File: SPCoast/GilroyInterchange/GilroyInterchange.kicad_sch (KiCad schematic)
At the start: 47 parts, among them SW783 783, SW795 795, SW799 799

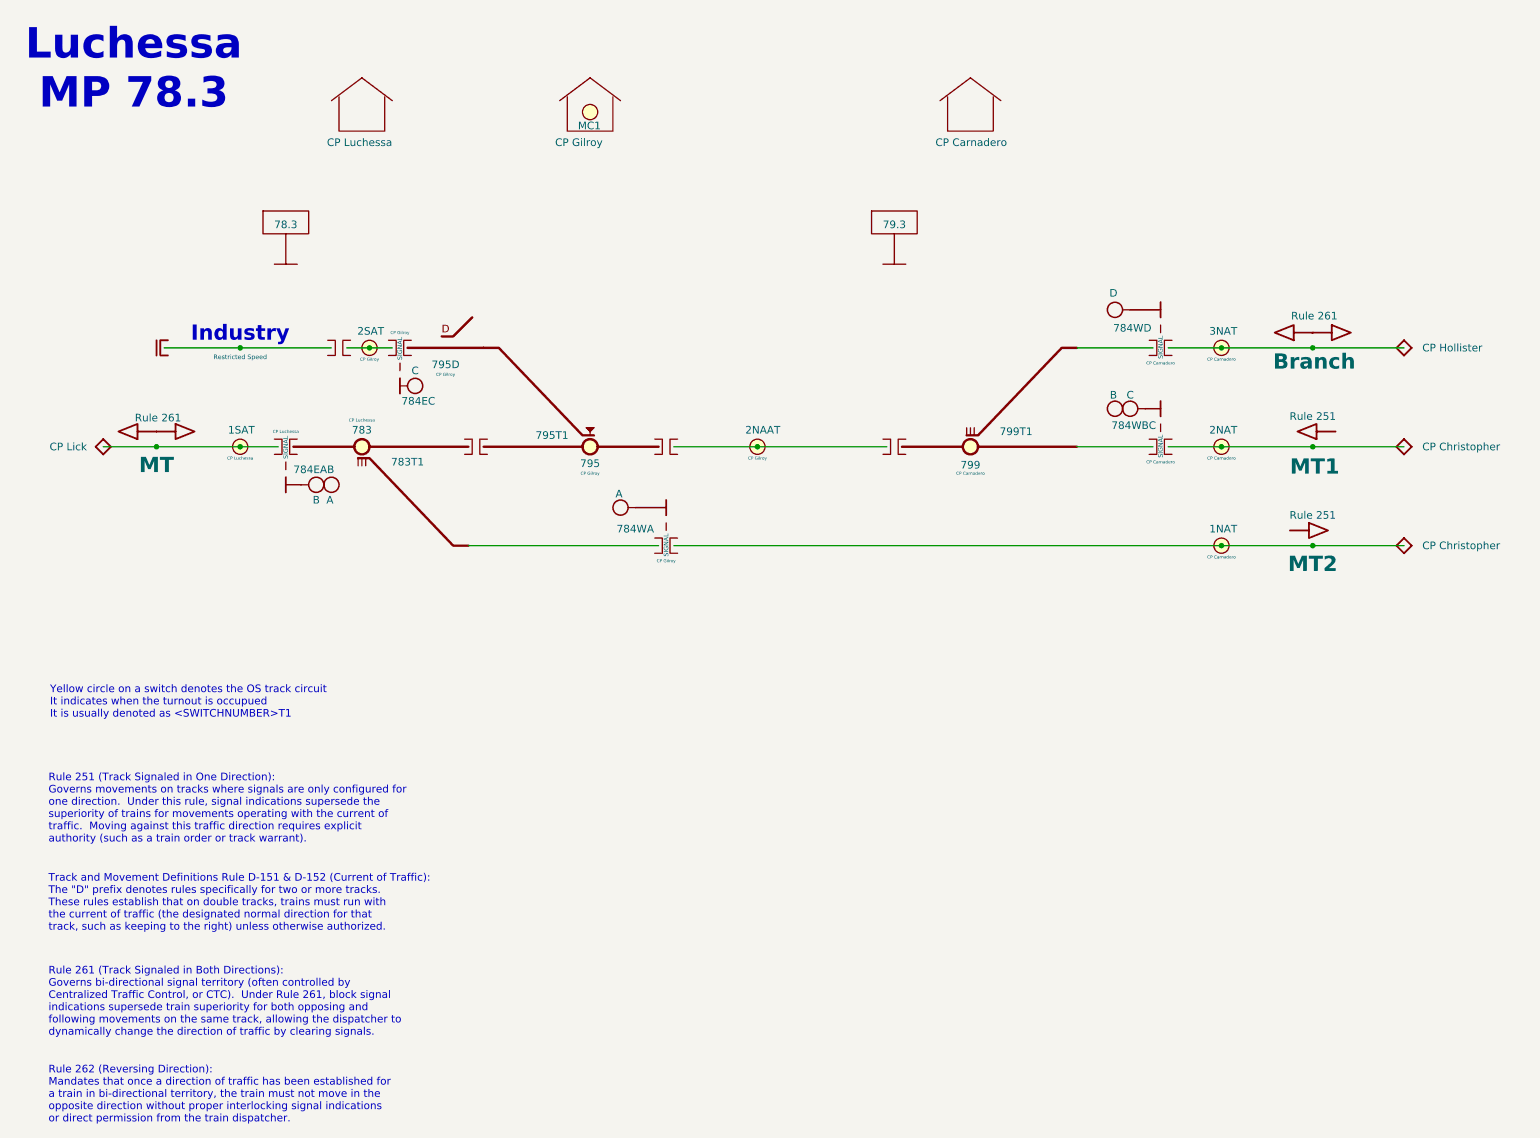
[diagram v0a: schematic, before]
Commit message: SPCoast: derail pin R, track circuit names end in T, code line symbols on the root sheet
Working-tree changes from the 2026-10-01..03 vocabulary review with
FieldUnit-Subdivision (docs/adr/0001-code-line-type-contract.md):

- Switch_Powered_Derail pin 2 is R (through path = REVERSE) in the seven
  plant schematics (library Railroad.kicad_sym renamed alongside; not in git)
- Luchessa track circuits renamed to end in T (1SAT, 2NAAT, ...); MC1 moved
  to CP Gilroy's house
- South-cTc: transports (MQTT, TimeCode, CMRInet, Loconet) on the root
  sheet on the CtcMachine Transports pin; field stations as encoding
  instances on the Luchessa sheet; two Luchessa lamp tokens renamed
- Six plant projects (Christopher, Corporal, GilroyCalTrain,
  GilroyInterchange, Sargent, Watsonville) added as drawn so far; Watsonville
  updated 2026-10-02

Co-Authored-By: Claude Fable 5.1 <noreply@anthropic.com>
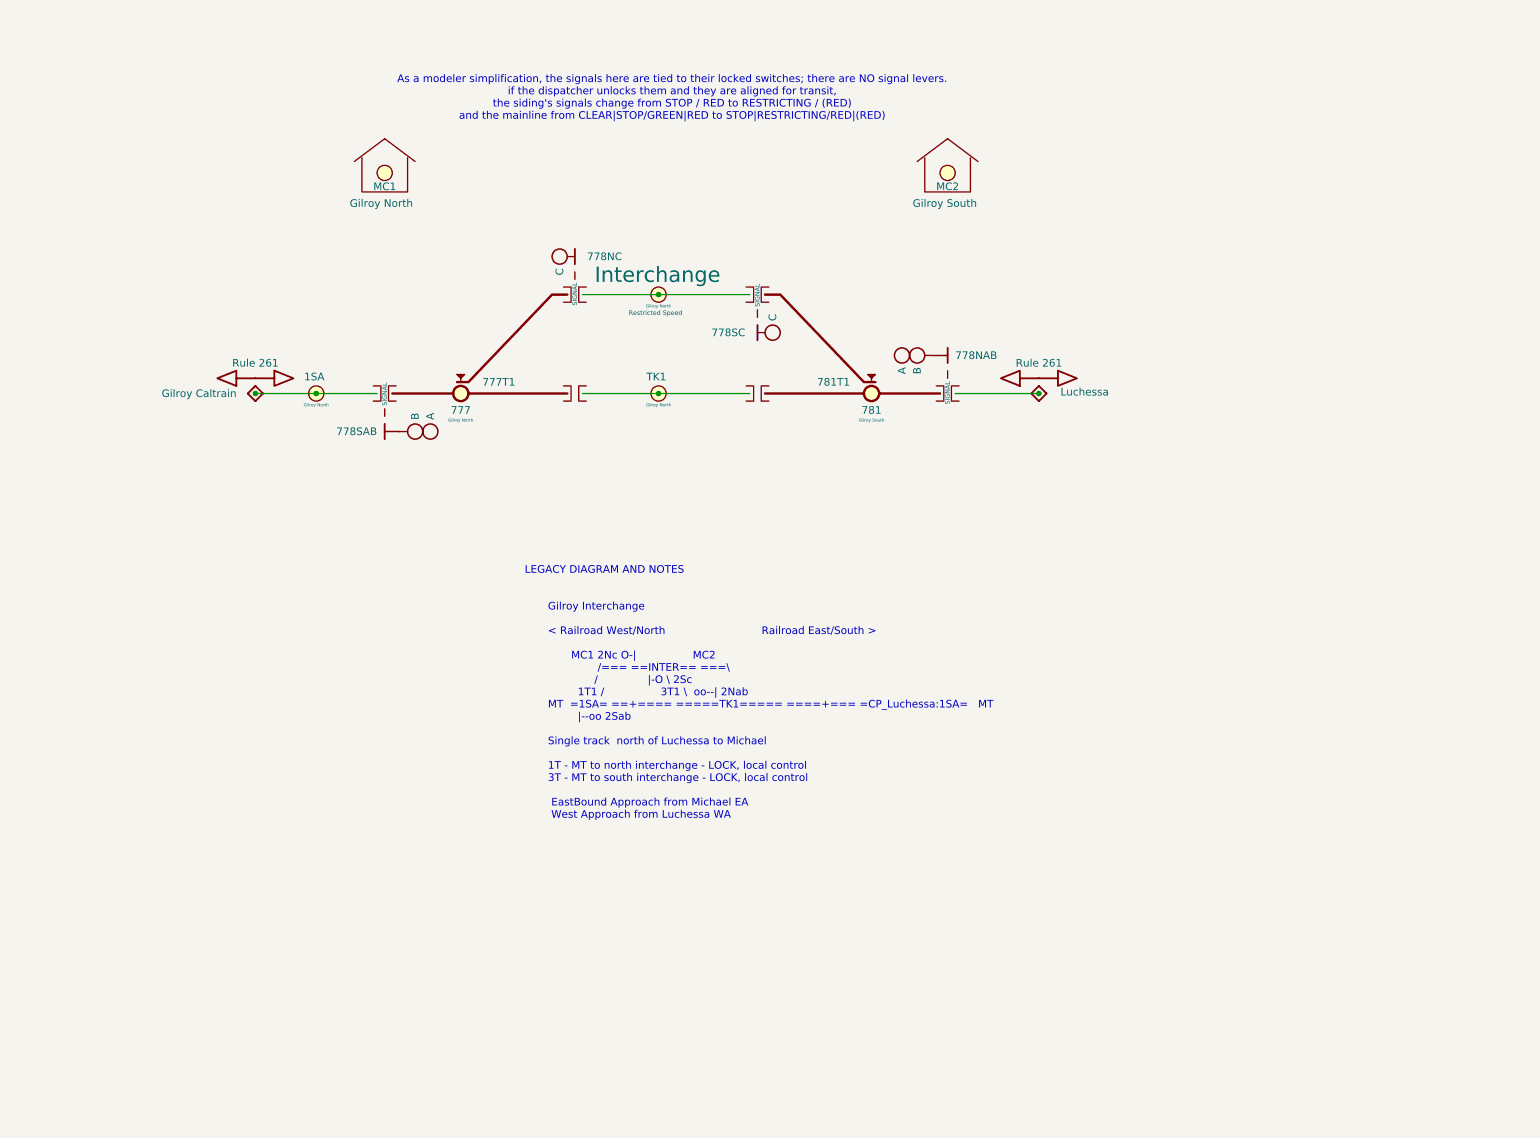
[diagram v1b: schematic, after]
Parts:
- removed B10, B2, B5, B6: (no value), symbol Railroad:IRJ
- removed B3, B4, B9: (no value), symbol Railroad:IRJ-Signal
- removed B7: (no value), symbol Railroad:Bumper
- removed CP3, CP4: CP Christopher, symbol Railroad:NextCP
- removed DERAIL795: 795D, symbol Railroad:Switch_Powered_Derail
- removed DOT1: MT1, symbol Railroad:Rule251-DoT-Left
- removed DOT2: MT2, symbol Railroad:Rule251-DoT-Right
- removed DOT3: MT, symbol Railroad:Rule261-DoT-BiDirectional
- removed DOT4: Branch, symbol Railroad:Rule261-DoT-BiDirectional
- removed DOT5: Restricted Speed, symbol Railroad:Rule105-RestrictedSpeed
- removed H7: B, symbol Railroad:Signal Head - CL
- removed H8: C, symbol Railroad:Signal Head - CL
- removed HOUSE3: CP Gilroy, symbol Railroad:MAIN HOUSE
- removed MP1: 79.3, symbol Railroad:Milepost
- removed MP2: 78.3, symbol Railroad:Milepost
- removed S784E1: 784EAB, symbol Railroad:Mast_Double
- removed S784E2: 784EC, symbol Railroad:Mast_Dwarf
- removed S784W1: 784WA, symbol Railroad:Mast_Single
- removed S784W2: 784WBC, symbol Railroad:Mast_Double
- removed S784W3: 784WD, symbol Railroad:Mast_Single
- removed SW783: 783, symbol Railroad:Switch_Powered
- removed SW795: 795, symbol Railroad:Switch_Lock
- removed SW799: 799, symbol Railroad:Switch_Powered
- removed TC4: 2NAAT, symbol Railroad:Track Circuit
- removed TC5: 2SAT, symbol Railroad:Track Circuit
- removed TC6: 1SAT, symbol Railroad:Track Circuit
- added B2, B7: (no value), symbol Railroad:IRJ-Signal
- added B3, B4: (no value), symbol Railroad:IRJ
- added DOT1, DOT2: Rule 261, symbol Railroad:Rule261-DoT-BiDirectional
- added DOT3: Restricted Speed, symbol Railroad:Rule105-RestrictedSpeed
- added H5: B, symbol Railroad:Signal Head - CL
- added MC2: MC2, symbol Railroad:MaintainerCall
- added S1: 778NC, symbol Railroad:Mast_Dwarf
- added S2: 778SC, symbol Railroad:Mast_Dwarf
- added S3: 778SAB, symbol Railroad:Mast_Double
- added S4: 778NAB, symbol Railroad:Mast_Double
- added SW777: 777, symbol Railroad:Switch_Lock
- added SW781: 781, symbol Railroad:Switch_Lock
- B1: CP CP Luchessa -> (none)
- B8: CP CP Carnadero -> (none)
- CP1: value CP Lick -> Gilroy Caltrain
- CP2: value CP Hollister -> Luchessa
- H1: value A -> C
- H2: value B -> C
- H3: value C -> A
- H4: value D -> B
- HOUSE1: value CP Luchessa -> Gilroy North; Milepost 78.3 -> 77.7
- HOUSE2: value CP Carnadero -> Gilroy South; Milepost 79.9 -> 78.1
- MC1: value (none) -> MC1; CP (none) -> Gilroy North
- TC1: value 3NAT -> 1SA; CP CP Carnadero -> Gilroy North
- TC2: value 2NAT -> TK1; CP CP Carnadero -> Gilroy North
- TC3: value 1NAT -> Interchange; CP CP Carnadero -> Gilroy North
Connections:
- net at H4.1 (M): now also S3.2 (H2)
- net at TC2.1 (MC): now also B3.2 (B), B4.1 (A); no longer B8.2 (B)
- net at H6.1 (M): now also S4.3 (H1)
- net at TC3.1 (MC): now also B1.2 (B), B2.2 (B), DOT3.1 (To)
- net at B8.3 (SIGNAL): now also S4.1 (SIGNAL)
- net at H3.1 (M): now also S3.3 (H1)
- net at MC1.1 (MC): now also HOUSE1.1 (H)
- net at B8.1 (A): now also SW781.1 (C)
- net at H1.1 (M): now also S1.2 (H)
- net at B1.1 (A): now also SW777.3 (R)
- net at TC1.1 (MC): now also CP1.1 (To), B7.2 (B), DOT2.1; no longer CP2.1 (To)
- net at H2.1 (M): now also S2.2 (H)
- net at HOUSE2.1 (H): now also MC2.1 (MC)
- net at B1.3 (SIGNAL): now also S1.1 (SIGNAL)
- new net: B7.1 (A), SW777.1 (C)
- new net: B7.3 (SIGNAL), S3.1 (SIGNAL)
- new net: B3.1 (A), SW777.2 (N)
- new net: B4.2 (B), SW781.2 (N)
- new net: B2.1 (A), SW781.3 (R)
- new net: H5.1 (M), S4.2 (H2)
- new net: B8.2 (B), CP2.1 (To), DOT1.1
- new net: B2.3 (SIGNAL), S2.1 (SIGNAL)
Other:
- note added: "As a modeler simplification, the signals here are tied to their locked switches; there are NO signal levers. if the dispatcher unlocks them and they are aligned for transit, the siding's signals change from STOP / RED to RESTRICTING / (RED) and the mainline from CLEAR|STOP/GREEN|RED to STOP|RESTRICTING/RED|(RED)"
- note added: "LEGACY DIAGRAM AND NOTES Gilroy Interchange < Railroad West/North Railroad East/South > MC1 2Nc O-| MC2 /=== ==INTER== ===\ / |-O \ 2Sc 1T1 / 3T1 \ oo--| 2Nab MT =1SA= ==+==== =====TK1===== ====+=== =CP_Luchessa:1SA= MT |--oo 2Sab Single track north of Luchessa to Michael 1T - MT to north interchange - LOCK, local control 3T - MT to south interchange - LOCK, local control EastBound Approach from 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"
- note removed: "Industry"
- note removed: "Luchessa MP 78.3"
- note removed: "Rule 251 (Track Signaled in One Direction): Governs movements on tracks where signals are only configured for one direction. Under this rule, signal indications supersede the superiority of trains for movements operating with the current of traffic. Moving against this traffic direction requires explicit authority (such as a train order or track warrant)."
- note removed: "Rule 261 (Track Signaled in Both Directions): Governs bi-directional signal territory (often controlled by Centralized Traffic Control, or CTC). Under Rule 261, block signal indications supersede train superiority for both opposing and following movements on the same track, allowing the dispatcher to dynamically change the direction of traffic by clearing signals."
- note removed: "Rule 262 (Reversing Direction): Mandates that once a direction of traffic has been established for a train in bi-directional territory, the train must not move in the opposite direction without proper interlocking signal indications or direct permission from the train dispatcher."
- note removed: "Track and Movement Definitions Rule D-151 & D-152 (Current of Traffic): The "D" prefix denotes rules specifically for two or more tracks. These rules establish that on double tracks, trains must run with the current of traffic (the designated normal direction for that track, such as keeping to the right) unless otherwise authorized."
- note removed: "Yellow circle on a switch denotes the OS track circuit It indicates when the turnout is occupued It is usually denoted as <SWITCHNUMBER>T1"
- title: Luchessa -> GilroyInterchange
